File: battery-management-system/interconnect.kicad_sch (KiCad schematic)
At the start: 3 parts, among them J21 rspro_header_5pin_3_5mm

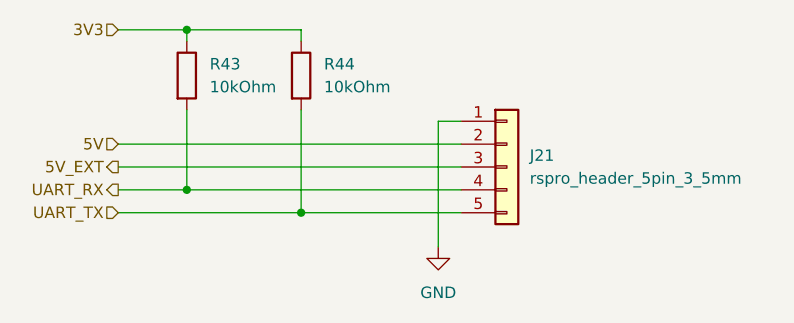
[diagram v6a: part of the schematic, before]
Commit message: add enable input for cell measurement
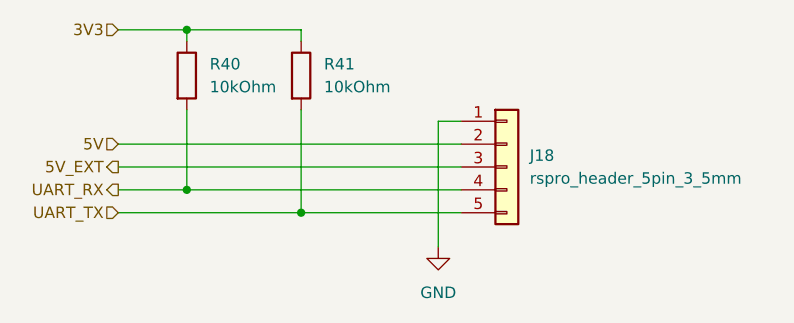
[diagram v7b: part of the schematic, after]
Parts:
- renumbered J21 to J18, R43 to R40, R44 to R41
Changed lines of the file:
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@@
   (symbol (lib_id "benediktibk:R_10kOhm_SMD_0603_100mW_1%") (at 41.91 21.59 0) (unit 1)
     (in_bom yes) (on_board yes) (dnp no) (fields_autoplaced)
-    (property "Reference" "R43" (at 44.45 20.3199 0)
+    (property "Reference" "R40" (at 44.45 20.3199 0)
       (effects (font (size 1.27 1.27)) (justify left))
     )
@@
       (project "battery-management-system"
         (path "/5272f0ff-3069-41a9-bca2-80beede8b4b2/3df28b0f-4877-411d-a6e0-0c6dff0863b2"
-          (reference "R43") (unit 1)
+          (reference "R40") (unit 1)
         )
       )
@@
   (symbol (lib_id "benediktibk:rspro_header_5pin_3_5mm") (at 77.47 31.75 0) (unit 1)
     (in_bom yes) (on_board yes) (dnp no) (fields_autoplaced)
-    (property "Reference" "J21" (at 80.01 30.48 0)
+    (property "Reference" "J18" (at 80.01 30.48 0)
       (effects (font (size 1.27 1.27)) (justify left))
     )
@@
       (project "battery-management-system"
         (path "/5272f0ff-3069-41a9-bca2-80beede8b4b2/3df28b0f-4877-411d-a6e0-0c6dff0863b2"
-          (reference "J21") (unit 1)
+          (reference "J18") (unit 1)
         )
       )
@@
   (symbol (lib_id "power:GND") (at 69.85 40.64 0) (unit 1)
     (in_bom yes) (on_board yes) (dnp no) (fields_autoplaced)
-    (property "Reference" "#PWR067" (at 69.85 46.99 0)
+    (property "Reference" "#PWR063" (at 69.85 46.99 0)
       (effects (font (size 1.27 1.27)) hide)
     )
@@
       (project "battery-management-system"
         (path "/5272f0ff-3069-41a9-bca2-80beede8b4b2/3df28b0f-4877-411d-a6e0-0c6dff0863b2"
-          (reference "#PWR067") (unit 1)
+          (reference "#PWR063") (unit 1)
         )
       )
@@
   (symbol (lib_id "benediktibk:R_10kOhm_SMD_0603_100mW_1%") (at 54.61 21.59 0) (unit 1)
     (in_bom yes) (on_board yes) (dnp no) (fields_autoplaced)
-    (property "Reference" "R44" (at 57.15 20.3199 0)
+    (property "Reference" "R41" (at 57.15 20.3199 0)
       (effects (font (size 1.27 1.27)) (justify left))
     )
@@
       (project "battery-management-system"
         (path "/5272f0ff-3069-41a9-bca2-80beede8b4b2/3df28b0f-4877-411d-a6e0-0c6dff0863b2"
-          (reference "R44") (unit 1)
+          (reference "R41") (unit 1)
         )
       )
